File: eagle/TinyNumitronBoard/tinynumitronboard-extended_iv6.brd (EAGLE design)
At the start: 100 x 50 mm, 37 parts

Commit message: Wiring continued
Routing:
- net N$134: track 0.00 -> 67.7 mm, vias 0 -> 6
- net N$121: track 0.00 -> 26.7 mm, vias 0 -> 2
- net N$131: track 0.00 -> 25.9 mm, vias 0 -> 1
- net N$133: track 0.00 -> 22.1 mm
- net N$113: track 0.00 -> 11.0 mm
- net N$110: track 28.0 -> 38.8 mm
- net N$159: track 0.00 -> 9.53 mm
- net N$158: track 0.00 -> 5.79 mm
- net VCC: track 249.9 -> 248.1 mm
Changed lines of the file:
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@@
 <wire x1="16.66875" y1="23.415625" x2="16.66875" y2="13.573125" width="0.1524" layer="1"/>
 <wire x1="16.66875" y1="13.573125" x2="16.66875" y2="7.62" width="0.1524" layer="1"/>
-<wire x1="16.66875" y1="7.62" x2="0.9525" y2="7.62" width="0.1524" layer="1"/>
-<wire x1="0.9525" y1="7.62" x2="0.9525" y2="17.78" width="0.1524" layer="1"/>
+<wire x1="16.66875" y1="7.62" x2="7.62" y2="7.62" width="0.1524" layer="1"/>
+<wire x1="7.62" y1="7.62" x2="6.35" y2="8.89" width="0.1524" layer="1"/>
+<wire x1="6.35" y1="8.89" x2="0.9525" y2="8.89" width="0.1524" layer="1"/>
+<wire x1="0.9525" y1="8.89" x2="0.9525" y2="17.78" width="0.1524" layer="1"/>
 <wire x1="0.9525" y1="17.78" x2="2.54" y2="17.78" width="0.1524" layer="1"/>
 <wire x1="36.83" y1="22.86" x2="35.639375" y2="22.86" width="0.1524" layer="1"/>
 <wire x1="35.639375" y1="22.86" x2="35.639375" y2="28.654375" width="0.1524" layer="1"/>
-<wire x1="35.639375" y1="28.654375" x2="36.83" y2="28.654375" width="0.1524" layer="1"/>
-<wire x1="36.83" y1="28.654375" x2="36.83" y2="31.75" width="0.1524" layer="1"/>
-<wire x1="36.83" y1="31.75" x2="36.83" y2="33.02" width="0.1524" layer="16"/>
+<wire x1="35.639375" y1="28.654375" x2="36.591875" y2="31.27375" width="0.1524" layer="1"/>
+<wire x1="36.591875" y1="31.27375" x2="36.591875" y2="31.75" width="0.1524" layer="1"/>
+<wire x1="36.591875" y1="31.75" x2="36.83" y2="33.02" width="0.1524" layer="16"/>
 <wire x1="36.83" y1="33.02" x2="38.735" y2="33.02" width="0.1524" layer="16"/>
 <wire x1="38.735" y1="33.02" x2="38.735" y2="35.321875" width="0.1524" layer="16"/>
 <wire x1="36.83" y1="33.02" x2="31.115" y2="33.02" width="0.1524" layer="16"/>
 <wire x1="31.115" y1="33.02" x2="31.115" y2="35.321875" width="0.1524" layer="16"/>
-<via x="36.83" y="31.75" extent="1-16" drill="0.3048"/>
+<via x="36.591875" y="31.75" extent="1-16" drill="0.3048"/>
 <wire x1="2.54" y1="17.78" x2="3.81" y2="17.78" width="0.1524" layer="16"/>
 <wire x1="3.81" y1="17.78" x2="3.81" y2="16.51" width="0.1524" layer="16"/>
@@
 </signal>
 <signal name="N$110">
-<wire x1="37.544375" y1="26.590625" x2="57.229375" y2="26.590625" width="0.1524" layer="1"/>
-<wire x1="57.229375" y1="26.590625" x2="57.229375" y2="23.495" width="0.1524" layer="1"/>
+<wire x1="37.94125" y1="31.670625" x2="57.229375" y2="31.670625" width="0.1524" layer="1"/>
+<wire x1="57.229375" y1="31.670625" x2="57.229375" y2="23.495" width="0.1524" layer="1"/>
 <wire x1="57.229375" y1="23.495" x2="62.38875" y2="23.495" width="0.1524" layer="1"/>
 <wire x1="62.38875" y1="23.495" x2="62.38875" y2="23.415625" width="0.1524" layer="1"/>
+<wire x1="37.94125" y1="31.670625" x2="36.83" y2="30.00375" width="0.1524" layer="1"/>
+<wire x1="36.83" y1="30.00375" x2="36.83" y2="26.67" width="0.1524" layer="1"/>
+<wire x1="36.83" y1="26.67" x2="37.544375" y2="26.590625" width="0.1524" layer="1"/>
 </signal>
 <signal name="N$111">
@@
 <wire x1="41.91" y1="1.27" x2="8.89" y2="1.27" width="0.1524" layer="16"/>
 <wire x1="8.89" y1="1.27" x2="8.89" y2="3.81" width="0.1524" layer="16"/>
-<wire x1="8.89" y1="3.81" x2="8.334375" y2="3.81" width="0.1524" layer="16"/>
-<wire x1="8.334375" y1="3.81" x2="8.334375" y2="8.493125" width="0.1524" layer="16"/>
+<wire x1="8.89" y1="3.81" x2="8.334375" y2="5.08" width="0.1524" layer="16"/>
+<wire x1="8.334375" y1="5.08" x2="8.334375" y2="8.493125" width="0.1524" layer="16"/>
 <wire x1="8.334375" y1="8.493125" x2="8.334375" y2="13.0175" width="0.1524" layer="1"/>
 <wire x1="8.334375" y1="13.0175" x2="9.525" y2="13.0175" width="0.1524" layer="16"/>
@@
 <via x="83.82" y="38.1" extent="1-16" drill="0.3048"/>
 </signal>
+<signal name="N$158">
+<wire x1="40.084375" y1="22.145625" x2="43.18" y2="22.145625" width="0.1524" layer="16"/>
+<wire x1="43.18" y1="22.145625" x2="43.18" y2="19.446875" width="0.1524" layer="16"/>
+</signal>
+<signal name="N$159">
+<wire x1="43.18" y1="18.57375" x2="48.10125" y2="18.57375" width="0.1524" layer="16"/>
+<wire x1="48.10125" y1="18.57375" x2="48.10125" y2="13.97" width="0.1524" layer="16"/>
+</signal>
+<signal name="N$113">
+<wire x1="38.496875" y1="19.923125" x2="36.83" y2="19.923125" width="0.1524" layer="16"/>
+<wire x1="36.83" y1="19.923125" x2="36.83" y2="17.78" width="0.1524" layer="16"/>
+<wire x1="36.83" y1="17.78" x2="33.655" y2="17.78" width="0.1524" layer="16"/>
+<wire x1="33.655" y1="17.78" x2="33.655" y2="13.81125" width="0.1524" layer="16"/>
+</signal>
+<signal name="N$121">
+<wire x1="29.289375" y1="25.003125" x2="27.94" y2="25.003125" width="0.1524" layer="16"/>
+<wire x1="27.94" y1="25.003125" x2="27.94" y2="20.32" width="0.1524" layer="16"/>
+<wire x1="27.94" y1="20.32" x2="27.94" y2="12.7" width="0.1524" layer="1"/>
+<wire x1="27.94" y1="12.7" x2="27.94" y2="12.144375" width="0.1524" layer="16"/>
+<wire x1="27.94" y1="12.144375" x2="38.735" y2="12.144375" width="0.1524" layer="16"/>
+<wire x1="38.735" y1="12.144375" x2="38.735" y2="13.81125" width="0.1524" layer="16"/>
+<via x="27.94" y="12.7" extent="1-16" drill="0.3048"/>
+<via x="27.94" y="20.32" extent="1-16" drill="0.3048"/>
+</signal>
+<signal name="N$133">
+<wire x1="40.005" y1="13.81125" x2="39.925625" y2="13.81125" width="0.1524" layer="16"/>
+<wire x1="39.925625" y1="13.81125" x2="39.925625" y2="20.6375" width="0.1524" layer="16"/>
+<wire x1="39.925625" y1="20.6375" x2="38.655625" y2="21.59" width="0.1524" layer="16"/>
+<wire x1="38.655625" y1="21.59" x2="31.75" y2="21.59" width="0.1524" layer="16"/>
+<wire x1="31.75" y1="21.59" x2="30.48" y2="24.13" width="0.1524" layer="16"/>
+<wire x1="30.48" y1="24.13" x2="30.48" y2="26.67" width="0.1524" layer="16"/>
+<wire x1="30.48" y1="26.67" x2="29.924375" y2="27.860625" width="0.1524" layer="16"/>
+</signal>
+<signal name="N$134">
+<wire x1="40.084375" y1="27.860625" x2="41.91" y2="27.94" width="0.1524" layer="16"/>
+<wire x1="41.91" y1="27.94" x2="43.18" y2="27.94" width="0.1524" layer="16"/>
+<wire x1="43.18" y1="27.94" x2="43.18" y2="25.4" width="0.1524" layer="16"/>
+<wire x1="43.18" y1="25.4" x2="43.18" y2="12.7" width="0.1524" layer="1"/>
+<wire x1="43.18" y1="12.7" x2="43.18" y2="2.54" width="0.1524" layer="16"/>
+<wire x1="43.18" y1="2.54" x2="40.9575" y2="2.143125" width="0.1524" layer="1"/>
+<via x="43.18" y="2.54" extent="1-16" drill="0.3048"/>
+<wire x1="40.9575" y1="2.143125" x2="26.67" y2="2.143125" width="0.1524" layer="16"/>
+<wire x1="26.67" y1="2.143125" x2="26.67" y2="2.54" width="0.1524" layer="16"/>
+<wire x1="26.67" y1="2.54" x2="26.67" y2="10.16" width="0.1524" layer="1"/>
+<wire x1="26.67" y1="10.16" x2="33.02" y2="10.16" width="0.1524" layer="1"/>
+<wire x1="33.02" y1="10.16" x2="33.02" y2="15.24" width="0.1524" layer="1"/>
+<wire x1="33.02" y1="15.24" x2="32.385" y2="15.954375" width="0.1524" layer="1"/>
+<wire x1="32.385" y1="15.954375" x2="32.385" y2="13.731875" width="0.1524" layer="16"/>
+<via x="32.385" y="15.954375" extent="1-16" drill="0.3048"/>
+<via x="26.67" y="2.54" extent="1-16" drill="0.3048"/>
+<via x="40.9575" y="2.143125" extent="1-16" drill="0.3048"/>
+<via x="43.18" y="12.7" extent="1-16" drill="0.3048"/>
+<via x="43.18" y="25.4" extent="1-16" drill="0.3048"/>
+</signal>
+<signal name="N$131">
+<wire x1="38.496875" y1="30.083125" x2="41.91" y2="29.21" width="0.1524" layer="1"/>
+<wire x1="41.91" y1="29.21" x2="41.91" y2="17.78" width="0.1524" layer="1"/>
+<wire x1="41.91" y1="17.78" x2="38.1" y2="17.78" width="0.1524" layer="1"/>
+<wire x1="38.1" y1="17.78" x2="38.1" y2="16.51" width="0.1524" layer="16"/>
+<wire x1="38.1" y1="16.51" x2="34.925" y2="16.51" width="0.1524" layer="16"/>
+<wire x1="34.925" y1="16.51" x2="34.925" y2="13.81125" width="0.1524" layer="16"/>
+<via x="38.1" y="17.78" extent="1-16" drill="0.3048"/>
+</signal>
 </signals>

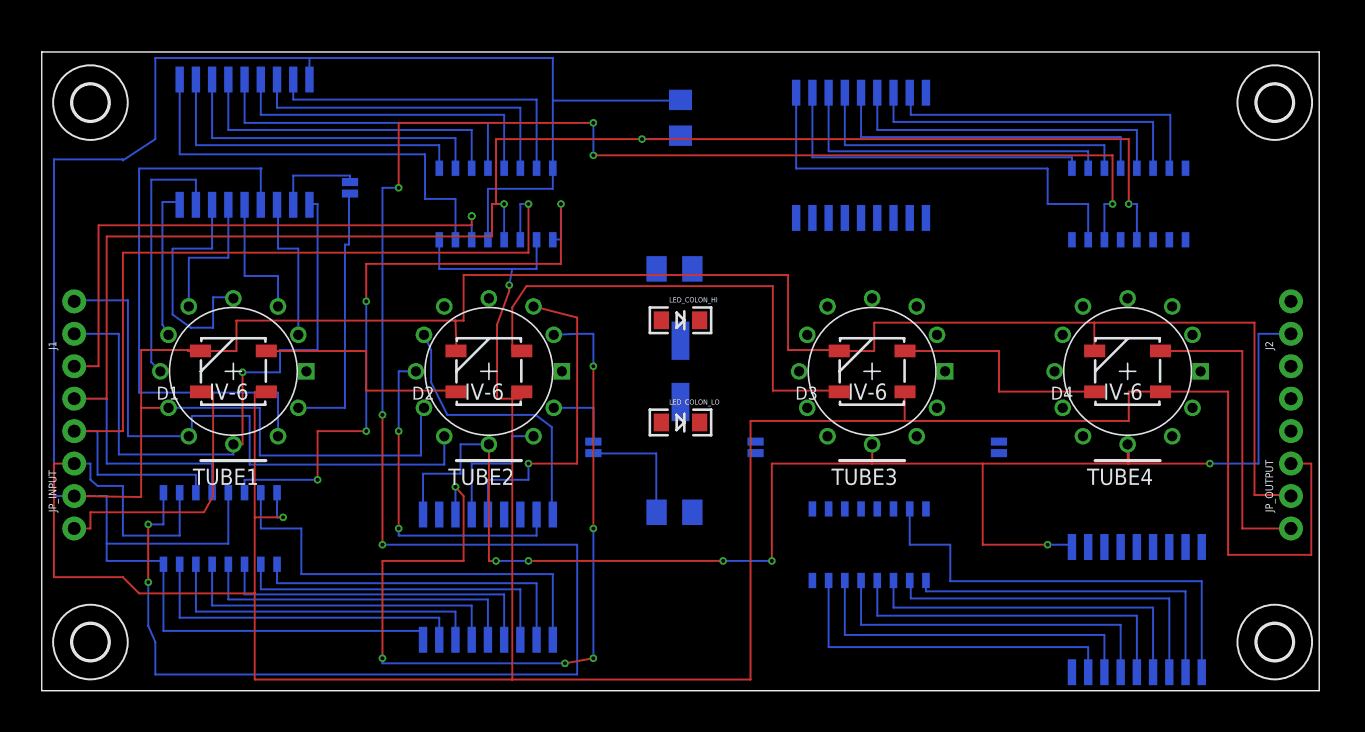
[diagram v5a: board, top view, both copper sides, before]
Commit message: After first pass of EagleGridFixer
Result look ok but in case
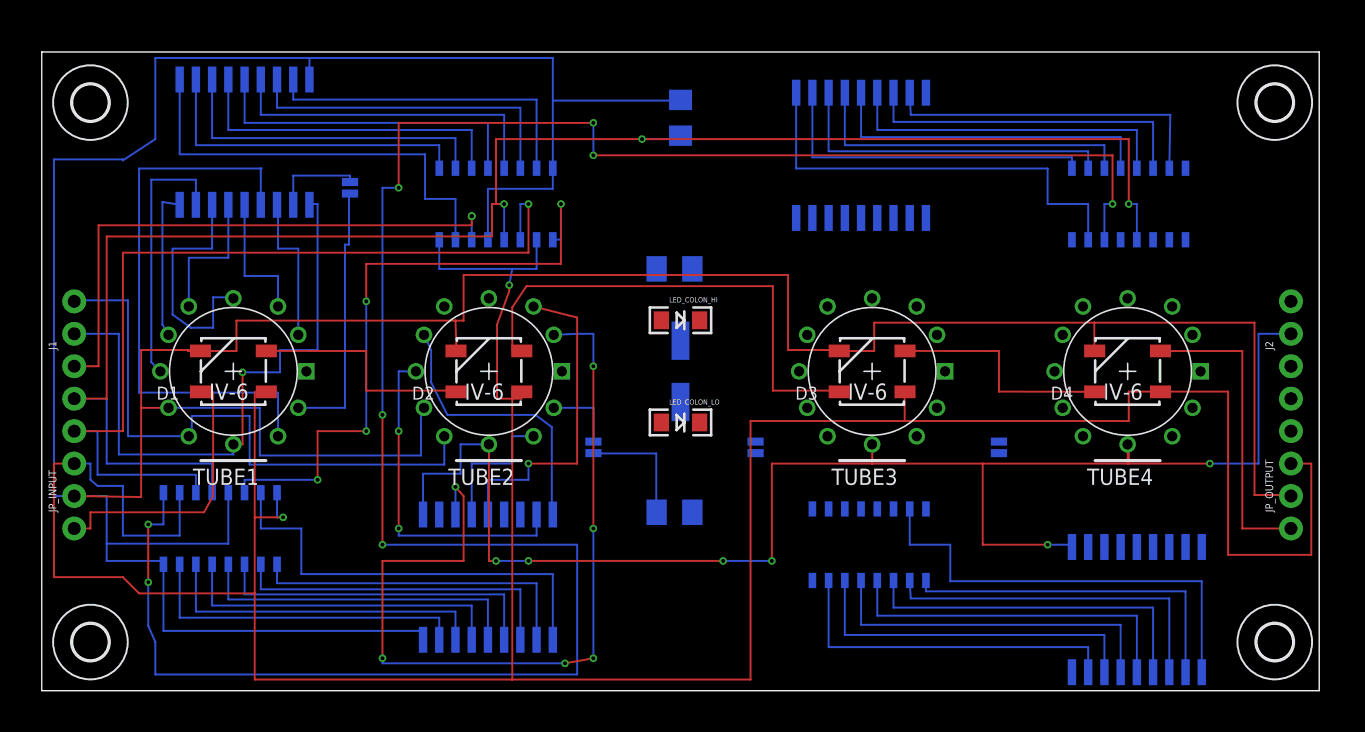
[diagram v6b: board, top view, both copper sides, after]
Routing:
- net N$13: track 0.00 -> 173.9 mm, vias 0 -> 8
- net N$142: track 173.9 -> 0.00 mm, vias 8 -> 0
- net N$134: track 67.7 -> 0.00 mm, vias 6 -> 0
- net N$42: track 0.00 -> 67.6 mm, vias 0 -> 6
- net N$137: track 50.8 -> 0.00 mm, vias 4 -> 0
- net N$23: track 0.00 -> 50.8 mm, vias 0 -> 4
- net N$56: track 0.00 -> 44.3 mm
- net N$122: track 44.1 -> 0.00 mm
- net N$10: track 0.00 -> 38.8 mm
- net N$110: track 38.8 -> 0.00 mm
- net N$32: track 0.00 -> 35.6 mm
- net N$128: track 35.6 -> 0.00 mm
- net N$126: track 34.4 -> 0.00 mm
- net N$66: track 0.00 -> 34.4 mm
- net N$44: track 0.00 -> 34.4 mm
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
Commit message: Wiring continued
Tube 3 ok, before running script for 2nd time
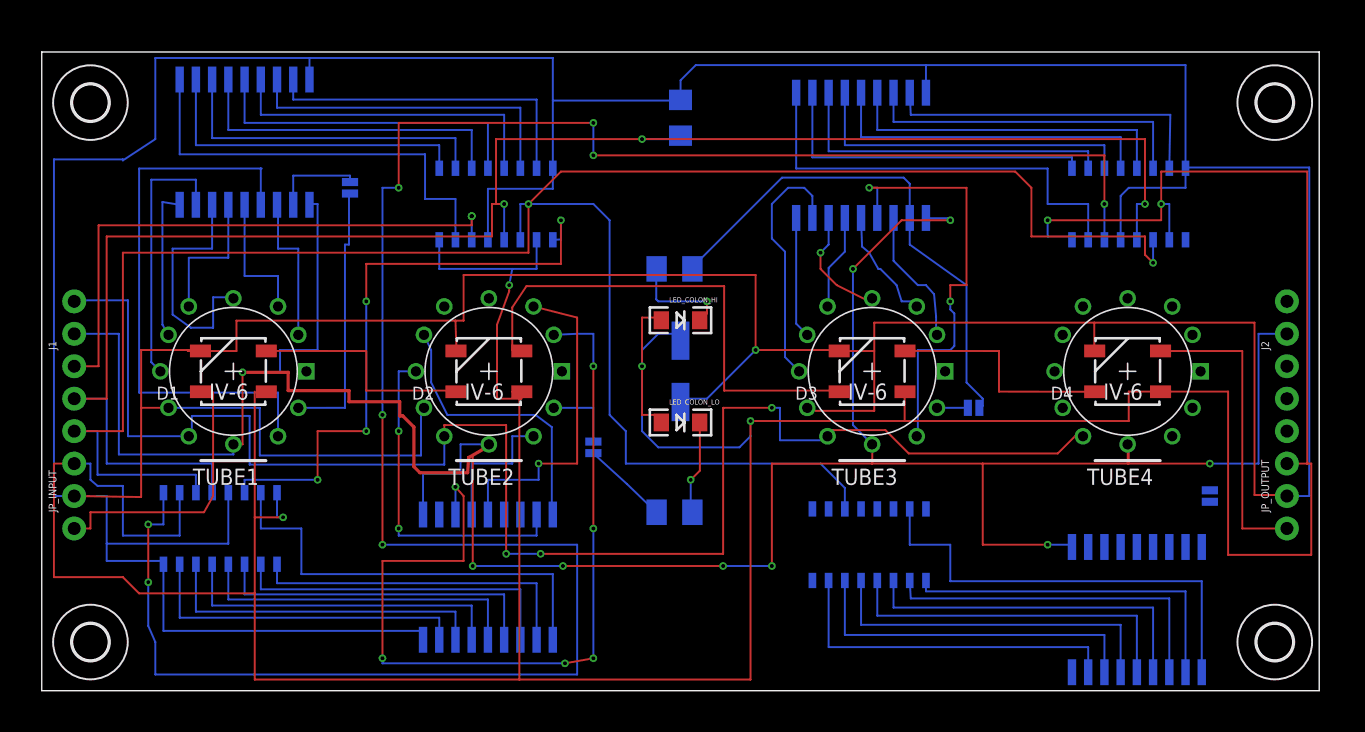
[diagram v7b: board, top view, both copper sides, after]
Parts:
- moved JP_DOT_TUBE3 17.3 mm to (72.9, 22.1), turned to 0 degrees
- moved JP_DOT_TUBE4 16.9 mm to (91.4, 15.2)
- moved J2 0.32 mm to (97.5, 27.9)
- moved JP_OUTPUT 0.32 mm to (97.5, 15.2)
- moved J_LED_OUT 0.32 mm to (97.5, 12.7)
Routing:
- net GND: track 299.0 -> 416.1 mm, vias 0 -> 1
- net SCK: track 71.2 -> 175.1 mm, vias 1 -> 2
- net VCC: track 248.1 -> 334.2 mm, vias 2 -> 6
- net GRID_P: track 107.7 -> 164.0 mm, vias 6 -> 7
- net N$88: track 0.00 -> 40.9 mm
- net N$99: track 0.00 -> 34.2 mm, vias 0 -> 2
- net N$20: track 26.1 -> 55.2 mm, vias 1 -> 3
- net N$89: track 0.00 -> 25.5 mm, vias 0 -> 2
- net N$96: track 0.00 -> 21.6 mm
- net N$82: track 0.00 -> 19.7 mm
- net N$87: track 0.00 -> 10.8 mm
- net N$81: track 0.00 -> 9.49 mm
- net N$84: track 0.00 -> 9.20 mm, vias 0 -> 1
- net N$86: track 0.00 -> 9.05 mm
- net N$94: track 0.00 -> 8.15 mm, vias 0 -> 1
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
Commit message: Before running script for 2nd time
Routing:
- net GND: track 416.1 -> 463.1 mm, vias 1 -> 3
- net N$105: track 0.00 -> 45.0 mm, vias 0 -> 2
- net RCK: track 138.3 -> 169.0 mm, vias 3 -> 5
- net SCK: track 175.1 -> 200.9 mm
- net VCC: track 334.2 -> 330.2 mm
